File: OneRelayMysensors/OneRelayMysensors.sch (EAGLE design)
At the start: 33 parts, among them IC1 MEGA328P-AU, Q1 32768hz, T1 BC847BW-7-F

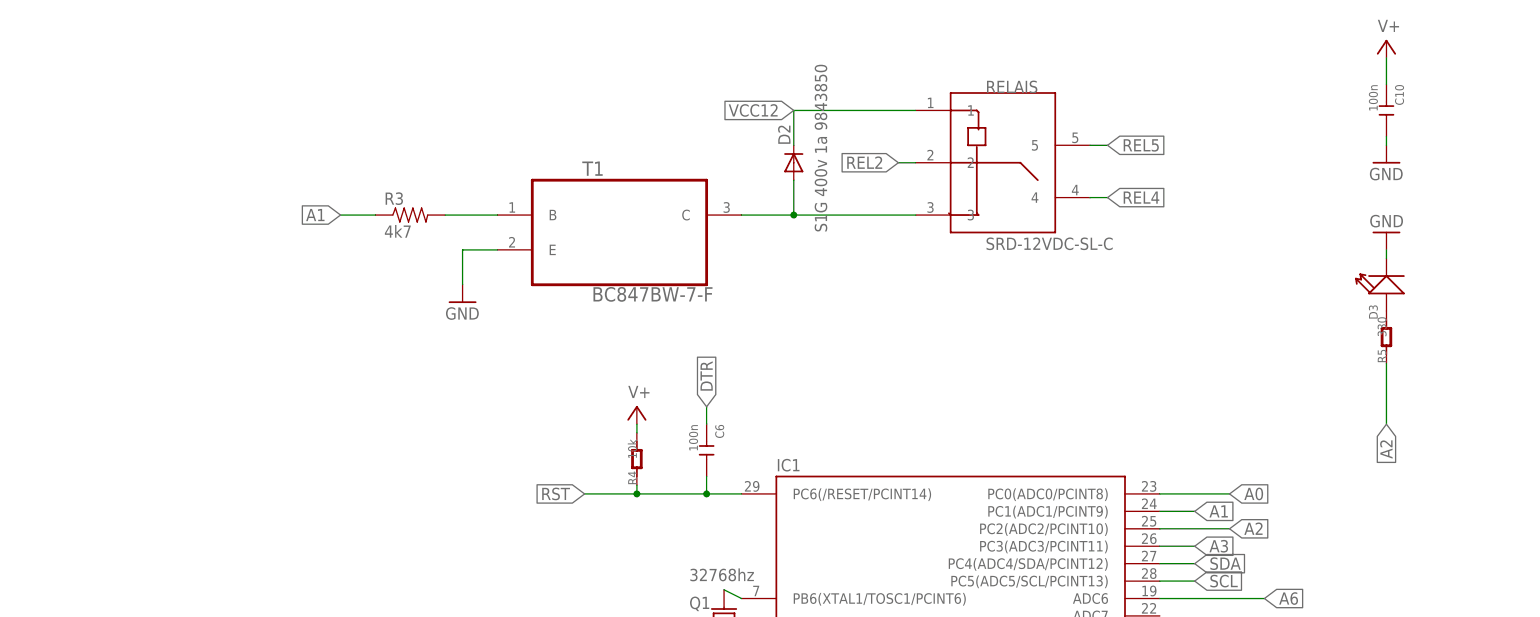
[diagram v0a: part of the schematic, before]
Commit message: relay footprint, changes res size
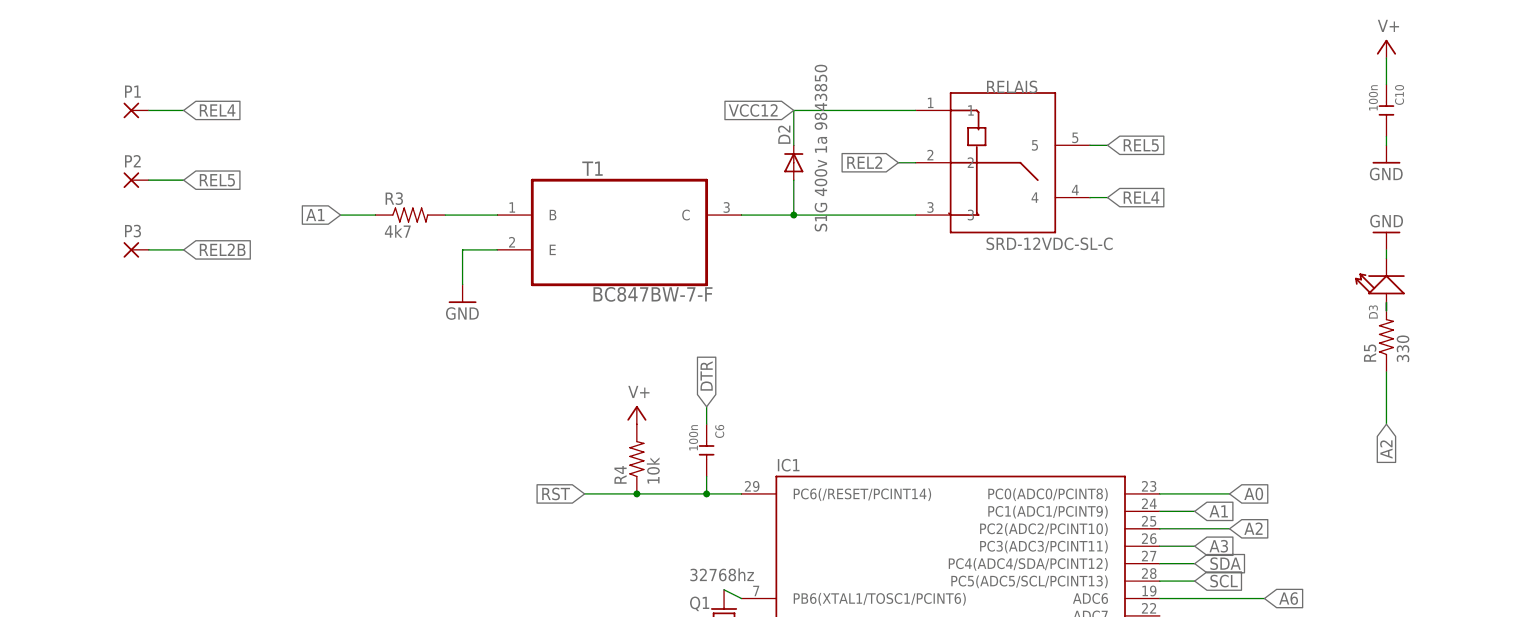
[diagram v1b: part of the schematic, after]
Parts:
- added P1, P2, P3: (no value), wirepad:2,54/1,1
- R4, R5: device Discrete:R-0805 -> SparkFun-Passives:RESISTOR1206
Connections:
- net REL2B: now also P3.P
- net REL4: now also P1.P
- net REL5: now also P2.P
